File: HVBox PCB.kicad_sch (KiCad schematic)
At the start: 15 parts, among them IC1 AS78L05RTR-E1, J1 43650-0516, J2 43650-0216, J3 43650-0416, J4 43650-0516, J5 43650-0316, J7 43650-0216, K1 HVR1B12

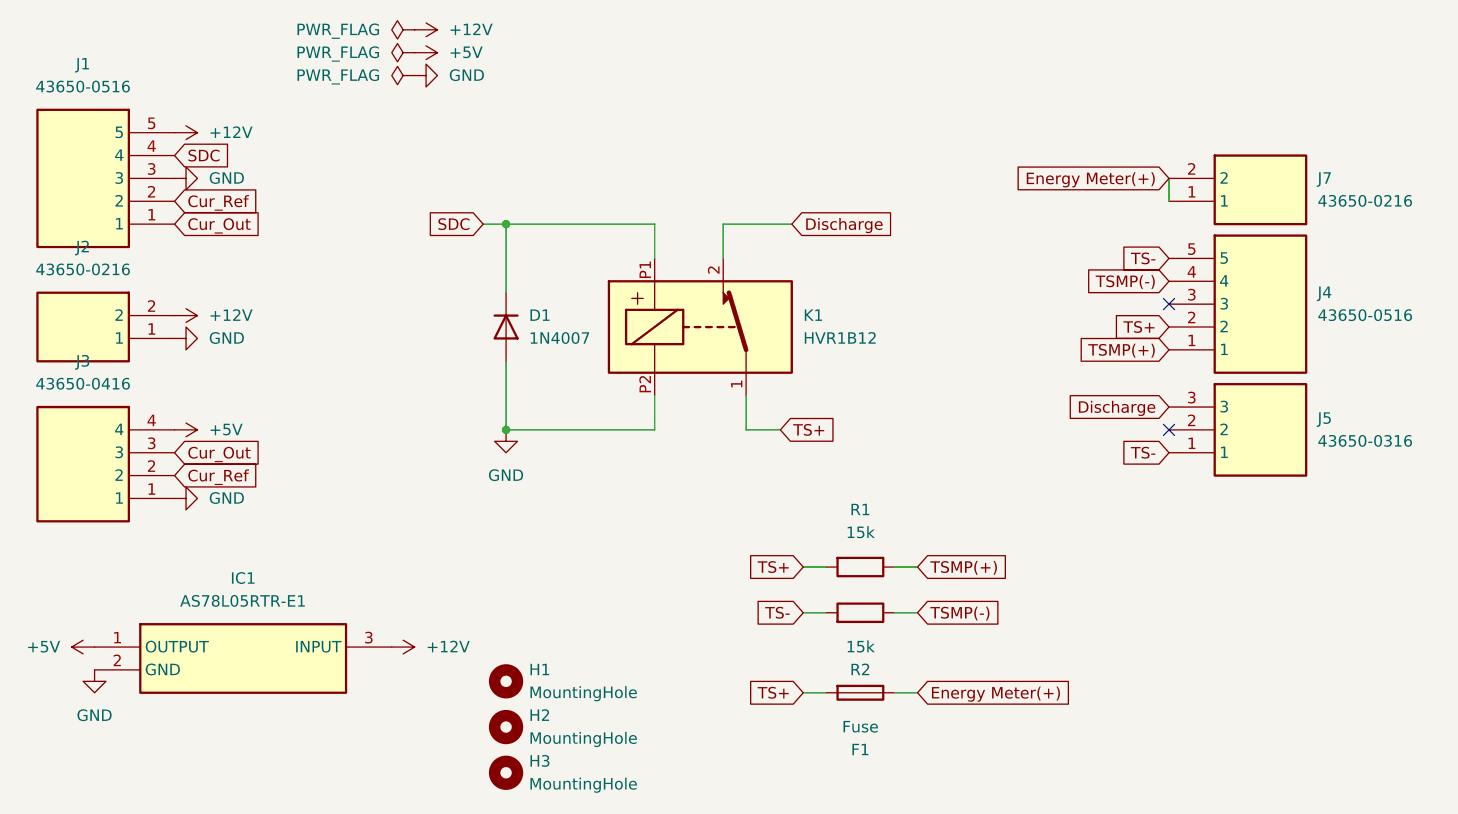
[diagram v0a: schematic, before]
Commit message: fix: mismatch of schema and pcb
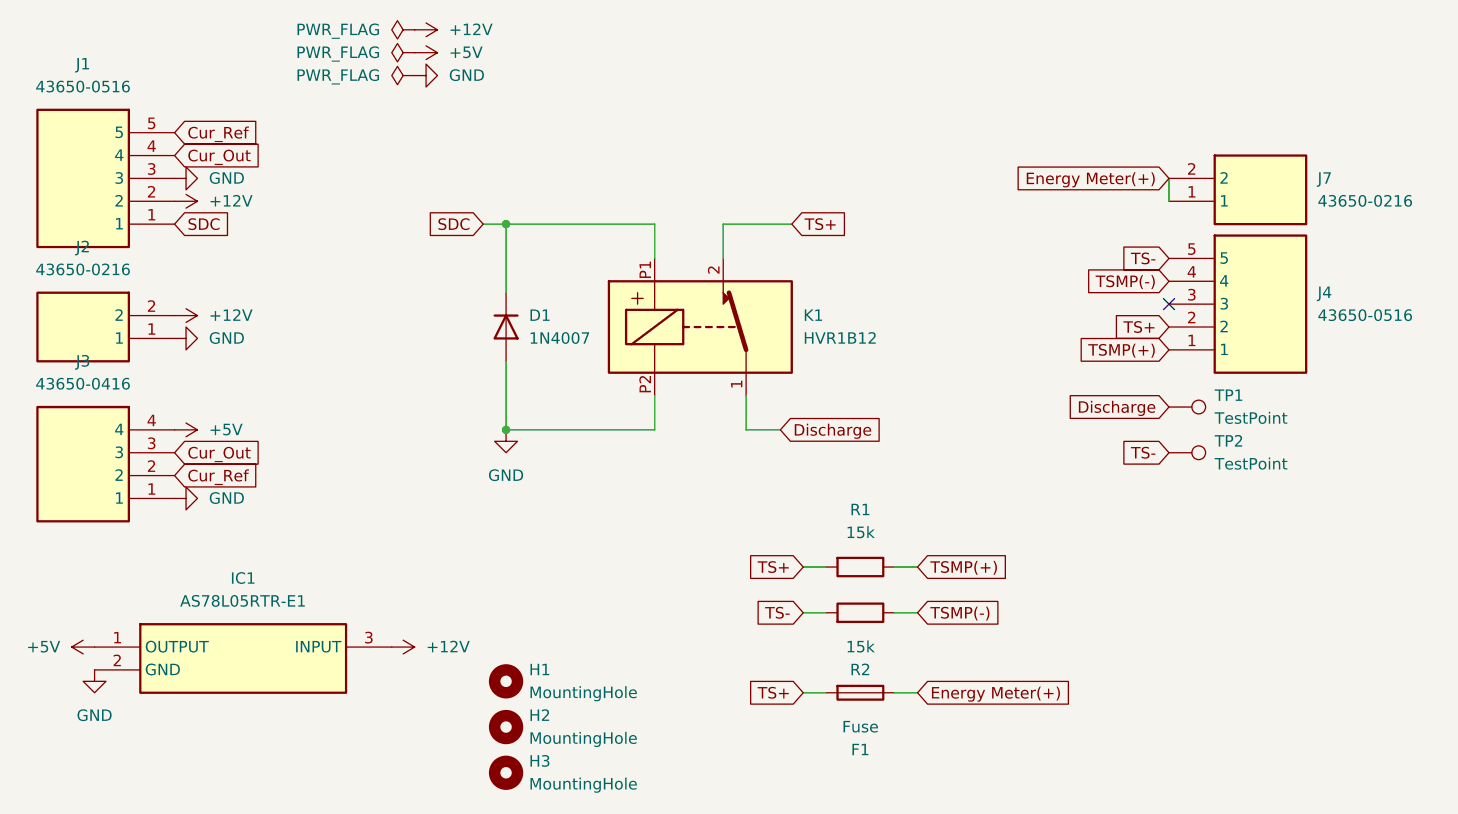
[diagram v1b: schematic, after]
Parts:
- removed J5: 43650-0316, Samacsys:43650-03YY_151617, symbol Samacsys:43650-0316
- added TP1, TP2: TestPoint, TestPoint:TestPoint_THTPad_D2.5mm_Drill1.2mm, symbol Connector:TestPoint
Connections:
- net +12V: now also J1.2; no longer J1.5
- net Cur_Out: now also J1.4; no longer J1.1
- net Cur_Ref: now also J1.5; no longer J1.2
- net Discharge: now also K1.1, TP1.1; no longer K1.2
- net SDC: now also J1.1; no longer J1.4
- net TS+: now also K1.2; no longer K1.1
- net TS-: now also TP2.1
- no-connect marks 2 -> 1
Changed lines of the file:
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@@
 		(at 186.69 86.36)
-	)
-	(no_connect
-		(at 186.69 100.33)
 	)
 	(wire
@@
 	(global_label "Cur_Out"
 		(shape input)
-		(at 76.2 77.47 0)
+		(at 76.2 69.85 0)
 		(fields_autoplaced yes)
 		(effects
@@
 		)
 		(property "Intersheetrefs" "${INTERSHEET_REFS}"
-			(at 86.5632 77.47 0)
+			(at 86.5632 69.85 0)
 			(effects
 				(font
@@
 	(global_label "Discharge"
 		(shape input)
-		(at 144.78 77.47 0)
+		(at 143.51 100.33 0)
 		(fields_autoplaced yes)
 		(effects
@@
 		)
 		(property "Intersheetrefs" "${INTERSHEET_REFS}"
-			(at 157.0785 77.47 0)
+			(at 155.8085 100.33 0)
 			(effects
 				(font
@@
 	(global_label "Cur_Ref"
 		(shape input)
-		(at 76.2 74.93 0)
+		(at 76.2 67.31 0)
 		(fields_autoplaced yes)
 		(effects
@@
 		)
 		(property "Intersheetrefs" "${INTERSHEET_REFS}"
-			(at 86.4423 74.93 0)
+			(at 86.4423 67.31 0)
 			(effects
 				(font
@@
 	(global_label "TS+"
 		(shape input)
-		(at 143.51 100.33 0)
+		(at 144.78 77.47 0)
 		(fields_autoplaced yes)
 		(effects
@@
 		)
 		(property "Intersheetrefs" "${INTERSHEET_REFS}"
-			(at 150.2447 100.33 0)
+			(at 151.5147 77.47 0)
 			(effects
 				(font
@@
 	(global_label "SDC"
 		(shape input)
-		(at 76.2 69.85 0)
+		(at 76.2 77.47 0)
 		(fields_autoplaced yes)
 		(effects
@@
 		)
 		(property "Intersheetrefs" "${INTERSHEET_REFS}"
-			(at 82.9347 69.85 0)
+			(at 82.9347 77.47 0)
 			(effects
 				(font
@@
 	(symbol
 		(lib_id "power:+12V")
-		(at 76.2 67.31 270)
+		(at 76.2 74.93 270)
 		(unit 1)
 		(exclude_from_sim no)
@@
 		(fields_autoplaced yes)
 		(property "Reference" "#PWR07"
-			(at 72.39 67.31 0)
+			(at 72.39 74.93 0)
 			(effects
 				(font
@@
 		)
 		(property "Value" "+12V"
-			(at 80.01 67.3099 90)
+			(at 80.01 74.9299 90)
 			(effects
 				(font
@@
 		)
 		(property "Footprint" ""
-			(at 76.2 67.31 0)
+			(at 76.2 74.93 0)
 			(effects
 				(font
@@
 		)
 		(property "Datasheet" ""
-			(at 76.2 67.31 0)
+			(at 76.2 74.93 0)
 			(effects
 				(font
@@
 		)
 		(property "Description" "Power symbol creates a global label with name \"+12V\""
-			(at 76.2 67.31 0)
+			(at 76.2 74.93 0)
 			(effects
 				(font
@@
 	)
 	(symbol
-		(lib_id "Samacsys:43650-0316")
-		(at 186.69 97.79 0)
-		(unit 1)
-		(exclude_from_sim no)
-		(in_bom yes)
-		(on_board yes)
-		(dnp no)
-		(fields_autoplaced yes)
-		(property "Reference" "J5"
-			(at 203.2 99.0599 0)
-			(effects
-				(font
-					(size 1.27 1.27)
-				)
-				(justify left)
-			)
-		)
-		(property "Value" "43650-0316"
-			(at 203.2 101.5999 0)
-			(effects
-				(font
-					(size 1.27 1.27)
-				)
-				(justify left)
-			)
-		)
-		(property "Footprint" "Samacsys:43650-03YY_151617"
-			(at 203.2 192.71 0)
-			(effects
-				(font
-					(size 1.27 1.27)
-				)
-				(justify left top)
-				(hide yes)
-			)
-		)
-		(property "Datasheet" "https://www.molex.com/pdm_docs/sd/436500215_sd.pdf"
-			(at 203.2 292.71 0)
-			(effects
-				(font
-					(size 1.27 1.27)
-				)
-				(justify left top)
-				(hide yes)
-			)
-		)
-		(property "Description" "Micro-Fit 3.0 Vertical Header, 3.00mm Pitch, Single Row, 3 Circuits, with PCB Polarizing Peg, Glow-Wire Capable, Black"
-			(at 186.69 97.79 0)
-			(effects
-				(font
-					(size 1.27 1.27)
-				)
-				(hide yes)
-			)
-		)
-		(property "Height" "9.9"
-			(at 203.2 492.71 0)
-			(effects
-				(font
-					(size 1.27 1.27)
-				)
-				(justify left top)
-				(hide yes)
-			)
-		)
-		(property "Mouser Part Number" "538-43650-0316"
-			(at 203.2 592.71 0)
-			(effects
-				(font
-					(size 1.27 1.27)
-				)
-				(justify left top)
-				(hide yes)
-			)
-		)
-		(property "Mouser Price/Stock" "https://www.mouser.co.uk/ProductDetail/Molex/43650-0316?qs=Nb99Pa9xYq8A2JEb2OZsGg%3D%3D"
-			(at 203.2 692.71 0)
-			(effects
-				(font
-					(size 1.27 1.27)
-				)
-				(justify left top)
-				(hide yes)
-			)
-		)
-		(property "Manufacturer_Name" "Molex"
-			(at 203.2 792.71 0)
-			(effects
-				(font
-					(size 1.27 1.27)
-				)
-				(justify left top)
-				(hide yes)
-			)
-		)
-		(property "Manufacturer_Part_Number" "43650-0316"
-			(at 203.2 892.71 0)
-			(effects
-				(font
-					(size 1.27 1.27)
-				)
-				(justify left top)
-				(hide yes)
-			)
-		)
-		(pin "1"
-		)
-		(pin "2"
-		)
-		(pin "3"
-		)
-		(instances
-			(project ""
-				(path "/5ab67901-fb3f-4046-b162-e1301107e96a"
-					(reference "J5")
-					(unit 1)
-				)
-			)
-		)
-	)
-	(symbol
 		(lib_id "power:PWR_FLAG")
 		(at 102.87 58.42 90)
@@
 	)
 	(symbol
+		(lib_id "Connector:TestPoint")
+		(at 186.69 97.79 270)
+		(unit 1)
+		(exclude_from_sim no)
+		(in_bom yes)
+		(on_board yes)
+		(dnp no)
+		(fields_autoplaced yes)
+		(property "Reference" "TP1"
+			(at 191.77 96.5199 90)
+			(effects
+				(font
+					(size 1.27 1.27)
+				)
+				(justify left)
+			)
+		)
+		(property "Value" "TestPoint"
+			(at 191.77 99.0599 90)
+			(effects
+				(font
+					(size 1.27 1.27)
+				)
+				(justify left)
+			)
+		)
+		(property "Footprint" "TestPoint:TestPoint_THTPad_D2.5mm_Drill1.2mm"
+			(at 186.69 102.87 0)
+			(effects
+				(font
+					(size 1.27 1.27)
+				)
+				(hide yes)
+			)
+		)
+		(property "Datasheet" "~"
+			(at 186.69 102.87 0)
+			(effects
+				(font
+					(size 1.27 1.27)
+				)
+				(hide yes)
+			)
+		)
+		(property "Description" "test point"
+			(at 186.69 97.79 0)
+			(effects
+				(font
+					(size 1.27 1.27)
+				)
+				(hide yes)
+			)
+		)
+		(pin "1"
+		)
+		(instances
+			(project ""
+				(path "/5ab67901-fb3f-4046-b162-e1301107e96a"
+					(reference "TP1")
+					(unit 1)
+				)
+			)
+		)
+	)
+	(symbol
 		(lib_id "power:+5V")
 		(at 76.2 100.33 270)
@@
 					(unit 1)
 				)
+			)
+		)
+	)
+	(symbol
+		(lib_id "Connector:TestPoint")
+		(at 186.69 102.87 270)
+		(unit 1)
+		(exclude_from_sim no)
+		(in_bom yes)
+		(on_board yes)
+		(dnp no)
+		(fields_autoplaced yes)
+		(property "Reference" "TP2"
+			(at 191.77 101.5999 90)
+			(effects
+				(font
+					(size 1.27 1.27)
+				)
+				(justify left)
+			)
+		)
+		(property "Value" "TestPoint"
+			(at 191.77 104.1399 90)
+			(effects
+				(font
+					(size 1.27 1.27)
+				)
+				(justify left)
+			)
+		)
+		(property "Footprint" "TestPoint:TestPoint_THTPad_D2.5mm_Drill1.2mm"
+			(at 186.69 107.95 0)
+			(effects
+				(font
+					(size 1.27 1.27)
+				)
+				(hide yes)
+			)
+		)
+		(property "Datasheet" "~"
+			(at 186.69 107.95 0)
+			(effects
+				(font
+					(size 1.27 1.27)
+				)
+				(hide yes)
+			)
+		)
+		(property "Description" "test point"
+			(at 186.69 102.87 0)
+			(effects
+				(font
+					(size 1.27 1.27)
+				)
+				(hide yes)
+			)
+		)
+		(pin "1"
+		)
+		(instances
+			(project "HVBox PCB"
+				(path "/5ab67901-fb3f-4046-b162-e1301107e96a"
+					(reference "TP2")
+					(unit 1)
+				)
